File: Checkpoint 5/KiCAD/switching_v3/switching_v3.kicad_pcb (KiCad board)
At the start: 2 copper layers, 140 x 110 mm, 61 parts, among them J1 Conn_01x02, J2 TP_BATT, J3 Conn_01x02, J4 TP_GND, J5 TP_GND, J6 TP_Cuad, J7 TP_Triang, J8 TP_Bootstrap, J9 TP_Vo, Q1 IRF740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

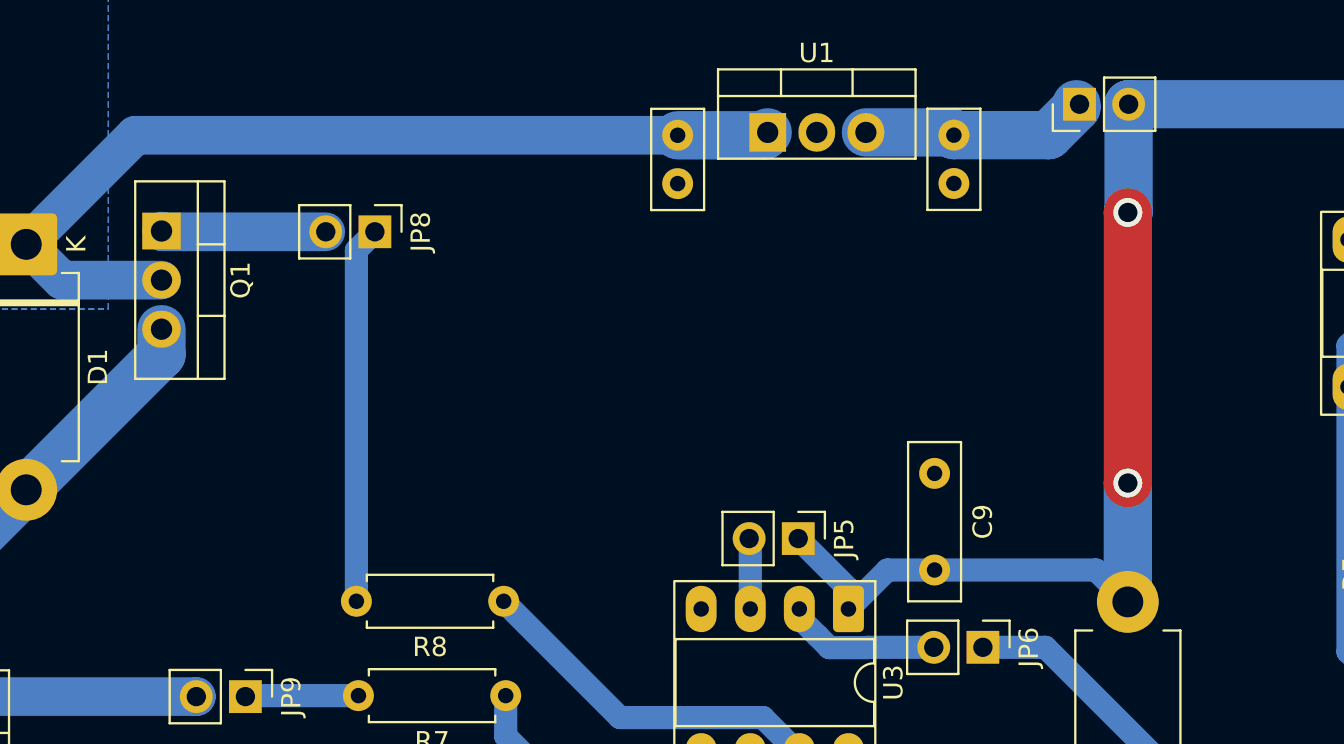
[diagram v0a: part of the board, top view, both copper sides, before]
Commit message: agregué el LM7810
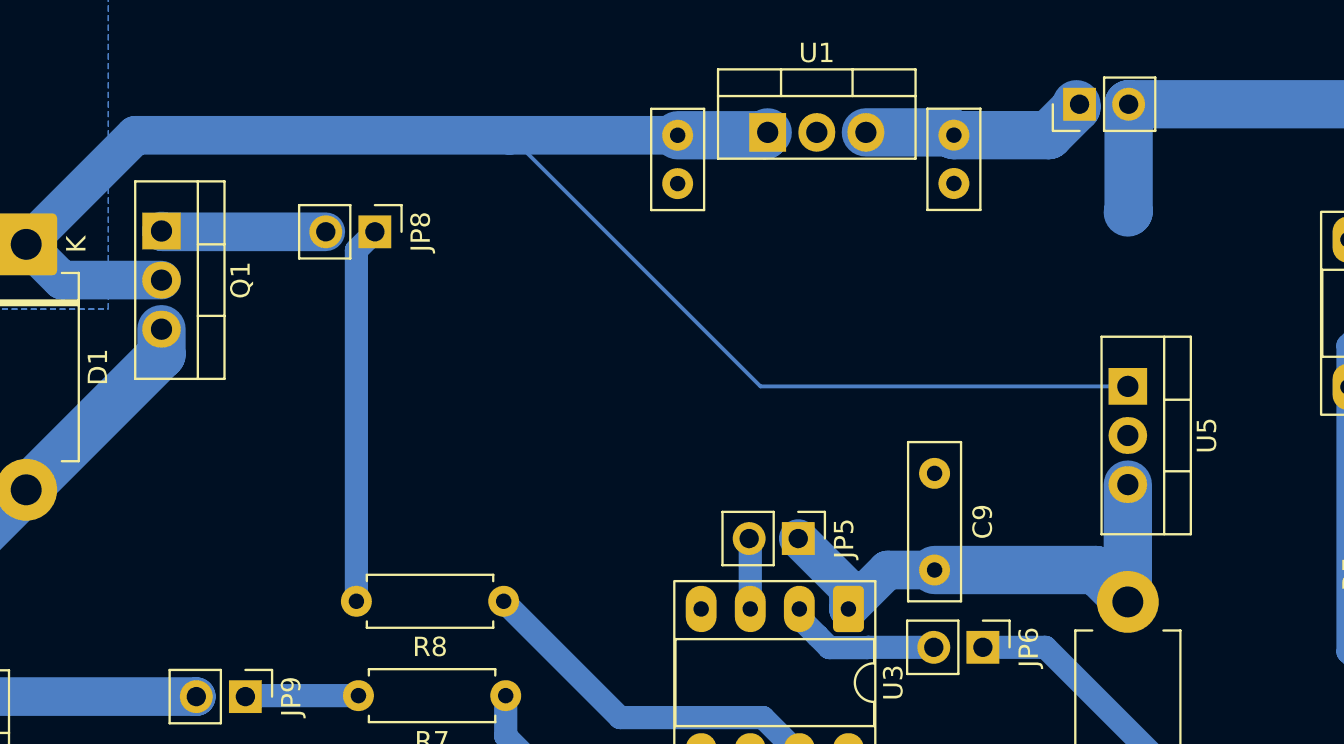
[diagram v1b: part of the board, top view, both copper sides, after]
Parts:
- added U5: LM7810_TO220, Package_TO_SOT_THT:TO-220-3_Vertical, F.Cu at (145.0, 56.0)
- R1, R2: value 560k -> 1Meg
- R10, R7, R8: value 1 -> 10
- R12, R4: value 470k -> 1Meg
- R3: value 4k7 -> 5k1
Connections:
- C9 pad 2: +9V -> Net-(D4-A)
- D4 pad 2: +9V -> Net-(D4-A)
- JP5 pad 1: +9V -> Net-(D4-A)
- U3 pad 1: +9V -> Net-(D4-A)
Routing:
- net +9V: track 257.9 -> 217.1 mm, vias 4 -> 2
- net +BATT: track 48.7 -> 86.1 mm
- net Net-(D4-A): track 0.00 -> 26.8 mm

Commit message: commit final
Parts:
- Cc2: value 1.2n -> 1.5n
- Cc3: value 5.6n -> 4.7n
